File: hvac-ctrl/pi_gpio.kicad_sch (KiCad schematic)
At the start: 26 parts

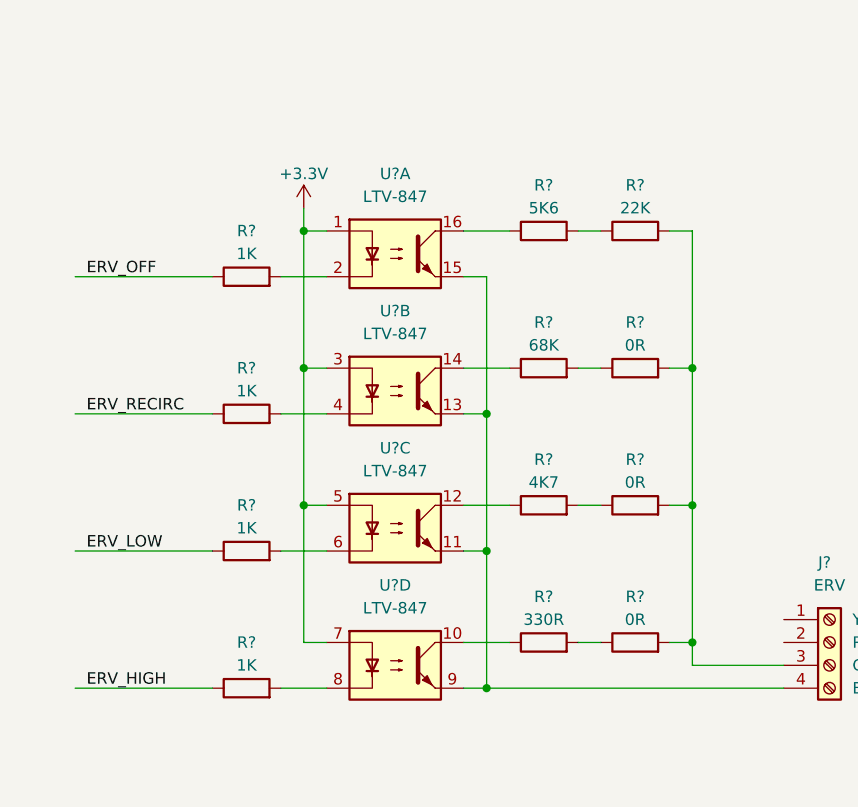
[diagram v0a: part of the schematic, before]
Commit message: ERV control block improvements
- add control LED to optocoupler input and adjust series resistor value
- update series resistor value for recirculating output
- add filter capacitor to output circuit
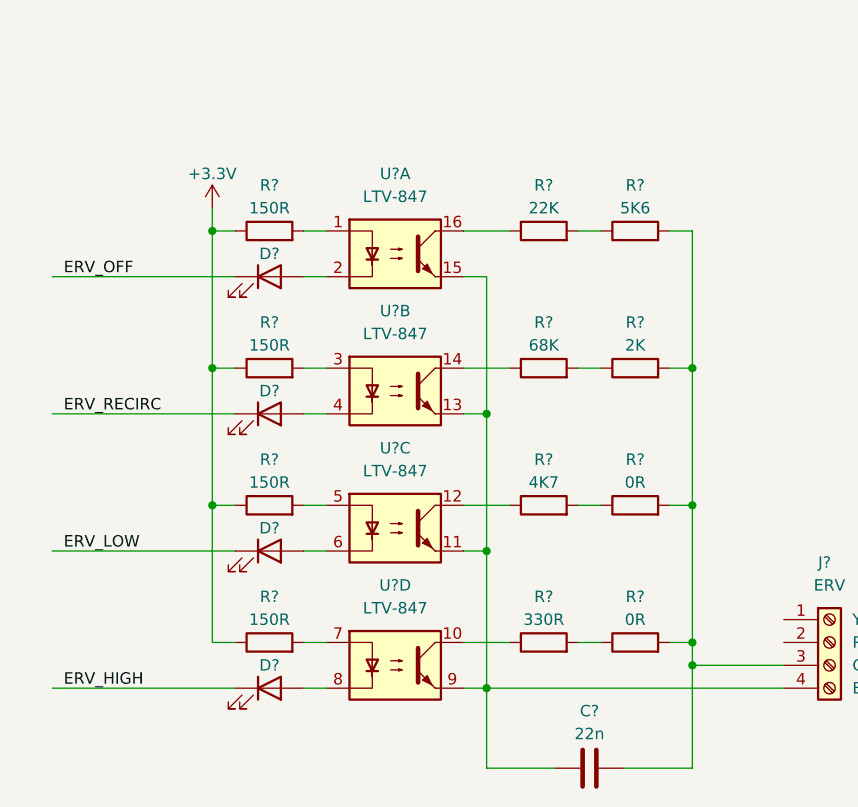
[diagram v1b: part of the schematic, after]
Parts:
- removed R? (x4): 1K, symbol Device:R
- added C?: 22n, symbol Device:C
- added D? (x4): LED, symbol Device:LED
- added R? (x4): 150R, symbol Device:R
- R?: value 22K -> 5K6
- R?: value 5K6 -> 22K
- R?: value 0R -> 2K
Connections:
- net +3.3V: now also R?.1, R?.1, R?.1, R?.1; no longer U?.1, U?.3, U?.5, U?.7
- net ERV_HIGH: now also D?.1 (K)
- net ERV_LOW: now also D?.1 (K)
- net ERV_OFF: now also D?.1 (K)
- net ERV_RECIRC: now also D?.1 (K)
- net at J?.3 (Pin_3), R?.2, R?.2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: now also C?.2
- net at U?.4: now also D?.2 (A)
- net at U?.8: now also D?.2 (A)
- net at J?.4 (Pin_4), U?.11, U?.13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: now also C?.1
- net at U?.2: now also D?.2 (A)
- net at U?.6: now also D?.2 (A)
- new net: R?.2, U?.1
- new net: R?.2, U?.7
- new net: R?.2, U?.5
- new net: R?.2, U?.3
